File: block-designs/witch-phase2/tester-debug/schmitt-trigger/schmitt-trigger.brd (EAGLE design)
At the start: 27.9 x 27.9 mm, 10 parts, among them IC1 74LVC1G14DBV

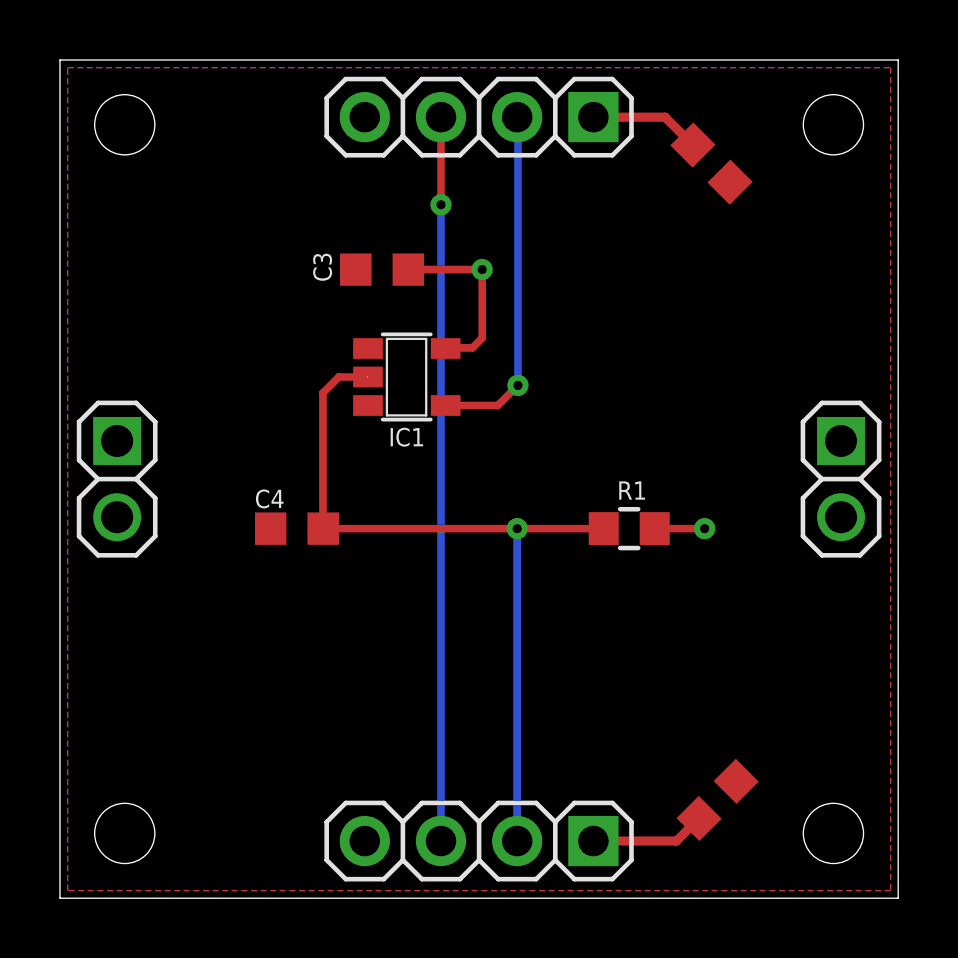
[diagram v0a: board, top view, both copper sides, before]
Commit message: change designs to use non-inverting schmitt triggers
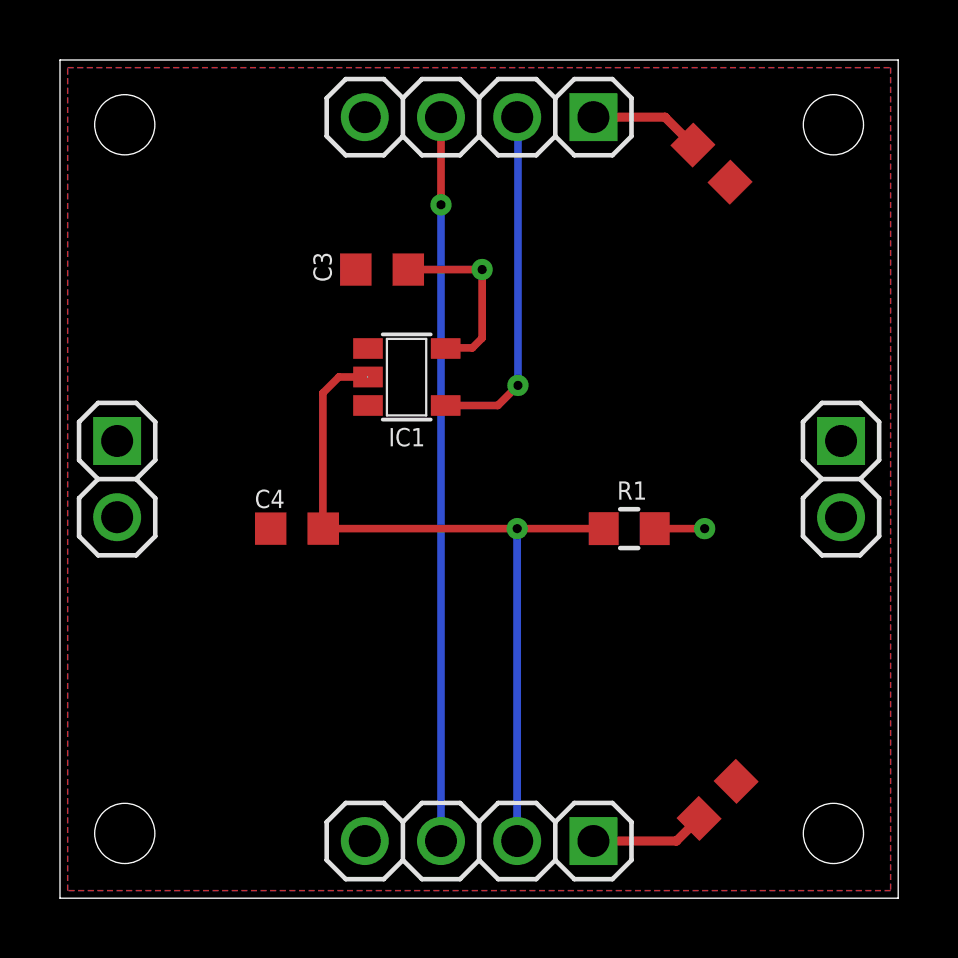
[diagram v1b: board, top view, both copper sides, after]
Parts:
- IC1: value 74LVC1G14DBV -> 74LVC1G17DBV
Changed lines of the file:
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@@
 <attribute name="VALUE" x="11.535309375" y="22.605" size="1.016" layer="27" rot="R180"/>
 </element>
-<element name="IC1" library="74xx-little-us" package="SOT23-5" value="74LVC1G14DBV" x="11.557" y="17.3736" smashed="yes" rot="R270">
+<element name="IC1" library="74xx-little-us" package="SOT23-5" value="74LVC1G17DBV" x="11.557" y="17.3736" smashed="yes" rot="R270">
 <attribute name="NAME" x="10.9474" y="15.0622" size="0.6096" layer="25"/>
 <attribute name="VALUE" x="7.747" y="19.9136" size="1.27" layer="27" rot="R270"/>
